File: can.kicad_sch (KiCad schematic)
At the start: 19 parts, among them J1 SM04B-GHS, J2 SM04B-GHS, Q1 Q_NMOS_GSD, U2 TJA1051TK/3/1J

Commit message: finish layout
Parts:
- Q1: symbol Device:Q_NMOS_GSD -> Transistor_FET:Q_NMOS_GSD
- U2: footprint Package_DFN_QFN:DFN-8-1EP_3x3mm_P0.65mm_EP1.55x2.4mm -> Package_SON:HVSON-8-1EP_3x3mm_P0.65mm_EP1.6x2.4mm
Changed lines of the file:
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@@
 	)
 	(junction
-		(at 73.66 53.34)
-		(diameter 0)
-		(color 0 0 0 0)
-	)
-	(junction
 		(at 184.15 39.37)
 		(diameter 0)
@@
 	(wire
 		(pts
-			(xy 72.39 52.07) (xy 72.39 53.34)
-		)
-		(stroke
-			(width 0)
-			(type default)
-		)
-	)
-	(wire
-		(pts
 			(xy 72.39 30.48) (xy 72.39 31.75)
 		)
@@
 	(wire
 		(pts
-			(xy 73.66 53.34) (xy 74.93 53.34)
-		)
-		(stroke
-			(width 0)
-			(type default)
-		)
-	)
-	(wire
-		(pts
 			(xy 41.91 36.83) (xy 41.91 34.29)
 		)
@@
 	(wire
 		(pts
-			(xy 73.66 53.34) (xy 73.66 54.61)
+			(xy 72.39 52.07) (xy 72.39 54.61)
 		)
 		(stroke
@@
 	(wire
 		(pts
-			(xy 74.93 52.07) (xy 74.93 53.34)
-		)
-		(stroke
-			(width 0)
-			(type default)
-		)
-	)
-	(wire
-		(pts
 			(xy 234.95 27.94) (xy 247.65 27.94)
 		)
@@
 	(wire
 		(pts
-			(xy 72.39 53.34) (xy 73.66 53.34)
-		)
-		(stroke
-			(width 0)
-			(type default)
-		)
-	)
-	(wire
-		(pts
 			(xy 242.57 53.34) (xy 247.65 53.34)
 		)
@@
 			)
 		)
-		(property "Description" ""
+		(property "Description" "Power symbol creates a global label with name \"GND\" , ground"
 			(at 106.68 52.07 0)
 			(effects
@@
 	)
 	(symbol
-		(lib_name "GND_2")
 		(lib_id "power:GND")
 		(at 234.95 43.18 0)
@@
 	)
 	(symbol
-		(lib_name "GND_2")
 		(lib_id "power:GND")
 		(at 240.03 43.18 0)
@@
 			)
 		)
-		(property "Description" ""
+		(property "Description" "Schottky diode"
 			(at 106.68 96.52 0)
 			(effects
@@
 			)
 		)
-		(property "Description" ""
+		(property "Description" "Resistor"
 			(at 41.91 40.64 0)
 			(effects
@@
 			)
 		)
-		(property "Description" ""
+		(property "Description" "Power symbol creates a global label with name \"GND\" , ground"
 			(at 120.65 52.07 0)
 			(effects
@@
 			)
 		)
-		(property "Description" ""
+		(property "Description" "Resistor"
 			(at 44.45 53.34 0)
 			(effects
@@
 	)
 	(symbol
-		(lib_id "Device:Q_NMOS_GSD")
+		(lib_id "Transistor_FET:Q_NMOS_GSD")
 		(at 181.61 54.61 0)
 		(unit 1)
@@
 			)
 		)
-		(property "Description" ""
+		(property "Description" "Power symbol creates a global label with name \"GND\" , ground"
 			(at 44.45 59.69 0)
 			(effects
@@
 	)
 	(symbol
-		(lib_name "GND_1")
 		(lib_id "power:GND")
 		(at 245.11 35.56 0)
@@
 			)
 		)
-		(property "Description" ""
+		(property "Description" "Unpolarized capacitor"
 			(at 106.68 45.72 0)
 			(effects
@@
 	)
 	(symbol
-		(lib_name "GND_1")
 		(lib_id "power:GND")
 		(at 252.73 68.58 0)
@@
 	)
 	(symbol
-		(lib_name "GND_1")
 		(lib_id "power:GND")
 		(at 245.11 63.5 0)
@@
 			)
 		)
-		(property "Footprint" "Package_DFN_QFN:DFN-8-1EP_3x3mm_P0.65mm_EP1.55x2.4mm"
+		(property "Footprint" "Package_SON:HVSON-8-1EP_3x3mm_P0.65mm_EP1.6x2.4mm"
 			(at 72.39 54.61 0)
 			(effects
@@
 			)
 		)
-		(property "Datasheet" "http://www.nxp.com/docs/en/data-sheet/TJA1051.pdf"
+		(property "Datasheet" "https://www.nxp.com/docs/en/data-sheet/TJA1051.pdf"
 			(at 72.39 41.91 0)
 			(effects
@@
 			)
 		)
-		(property "Description" ""
+		(property "Description" "High-Speed CAN Transceiver, separate VIO, silent mode, VSON-8 (DFN-8)"
 			(at 72.39 41.91 0)
 			(effects
@@
 	)
 	(symbol
-		(lib_name "GND_1")
 		(lib_id "power:GND")
 		(at 252.73 40.64 0)
@@
 	(symbol
 		(lib_id "power:GND")
-		(at 73.66 54.61 0)
+		(at 72.39 54.61 0)
 		(unit 1)
 		(exclude_from_sim no)
@@
 		(fields_autoplaced yes)
 		(property "Reference" "#PWR013"
-			(at 73.66 60.96 0)
+			(at 72.39 60.96 0)
 			(effects
 				(font
@@
 		)
 		(property "Value" "GND"
-			(at 73.66 59.69 0)
+			(at 72.39 59.69 0)
 			(effects
 				(font
@@
 		)
 		(property "Footprint" ""
-			(at 73.66 54.61 0)
+			(at 72.39 54.61 0)
 			(effects
 				(font
@@
 		)
 		(property "Datasheet" ""
-			(at 73.66 54.61 0)
+			(at 72.39 54.61 0)
 			(effects
 				(font
@@
 			)
 		)
-		(property "Description" ""
-			(at 73.66 54.61 0)
+		(property "Description" "Power symbol creates a global label with name \"GND\" , ground"
+			(at 72.39 54.61 0)
 			(effects
 				(font
@@
 			)
 		)
-		(property "Description" ""
+		(property "Description" "Unpolarized capacitor"
 			(at 120.65 45.72 0)
 			(effects

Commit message: improvements with derick
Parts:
- TP5: now left out of the parts list
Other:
- note added: "Next revision: increase ESD footprint size"
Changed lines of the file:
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@@
+		)
+	)
+	(text "Next revision: increase ESD footprint size"
+		(exclude_from_sim no)
+		(at 238.252 22.352 0)
+		(effects
+			(font
+				(size 1.27 1.27)
+			)
 		)
 	)
@@
 		(unit 1)
 		(exclude_from_sim no)
-		(in_bom yes)
+		(in_bom no)
 		(on_board yes)
 		(dnp no)

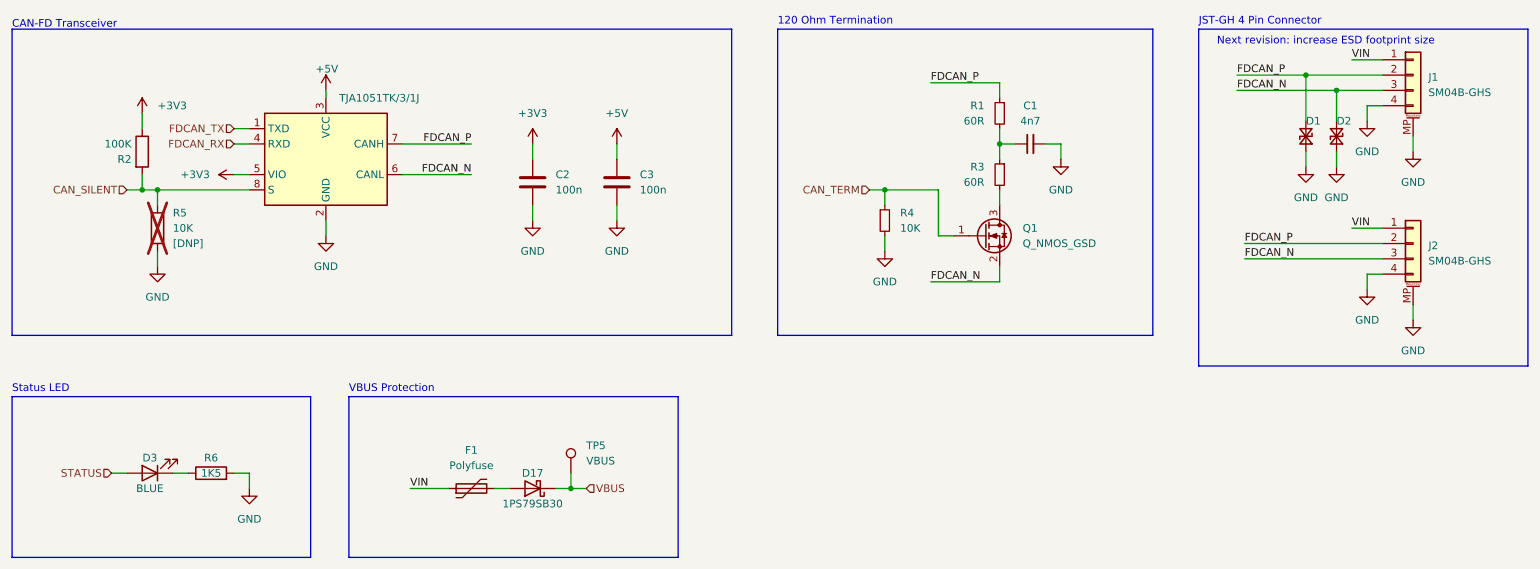
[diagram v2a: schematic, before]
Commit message: updated layout for fault led with new circuit, rerouted
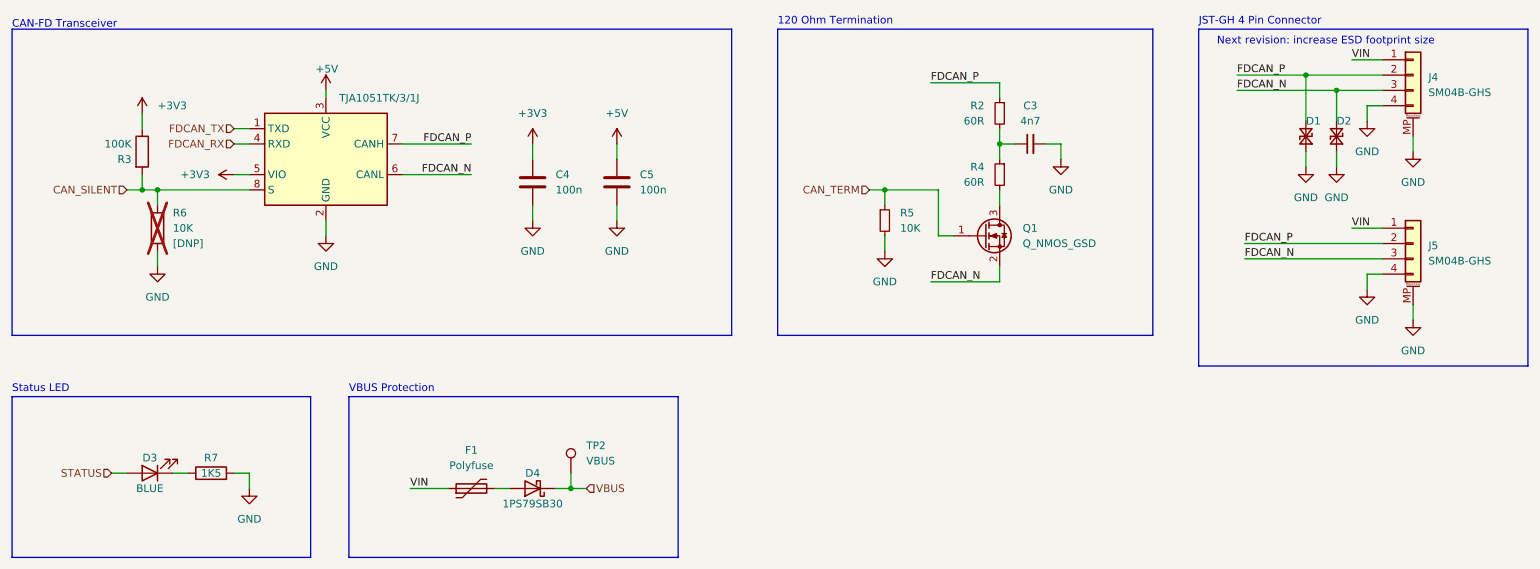
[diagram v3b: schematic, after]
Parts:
- renumbered C1 to C3, C2 to C4, C3 to C5, D17 to D4, J1 to J4, J2 to J5, R1 to R2, R2 to R3, R3 to R4, R4 to R5, R5 to R6, R6 to R7, TP5 to TP2
